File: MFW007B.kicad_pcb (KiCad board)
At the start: 4 copper layers, 84 x 42 mm, 63 parts, among them SW1 SW_Push, SW2 SW_Push, SW3 SW_Push, SW4 SW_Push, U1 24AA02-OT, U2 W5500, U3 STM32F103C8T6, Y1 25MHz

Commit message: update 2021-03-25
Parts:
- added U4: XC6206P332MR-G-SOT23, Package_TO_SOT_SMD:SOT-23, F.Cu at (169.0, 42.0)
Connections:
- net no_connect_(U3-Pad3) renamed /MCU/OSC32_IN
- net no_connect_(U3-Pad4) renamed /MCU/OSC32_OUT
- net no_connect_(U3-Pad5) renamed /MCU/OSC_IN
- net no_connect_(U3-Pad6) renamed /MCU/OSC_OUT

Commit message: fix label assignments and add 2x7 header
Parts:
- added J1: Conn_01x04, Connector_PinHeader_2.54mm:PinHeader_1x04_P2.54mm_Vertical, F.Cu at (170.5, 105.5)
- added J2: Conn_02x07, Connector_PinHeader_2.54mm:PinHeader_2x07_P2.54mm_Vertical, F.Cu at (164.5, 116.8)
- added J3: 4P JST-SH, Connector_JST:JST_SH_SM04B-SRSS-TB_1x04-1MP_P1.00mm_Horizontal, F.Cu at (169.0, 89.2)
- added TP1: TAMPER-RTC, TestPoint:TestPoint_Keystone_5010-5014_Multipurpose, F.Cu at (134.8, 118.2)
- added U5: TPS23753APWR, TPS23753APWR:SOP65P640X120-14N, F.Cu at (41.5, 42.5)
- moved U3 60.2 mm to (151.2, 107.5), turned to 180 degrees
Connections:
- net no_connect_(U3-Pad10) renamed /MCU/PA0_WKUP
- net no_connect_(U3-Pad20) renamed /MCU/BOOT1
- net no_connect_(U3-Pad44) renamed /MCU/BOOT0
- net no_connect_(U3-Pad7) renamed /MCU/NRST
- C10 pad 1: no_connect_(C10-Pad1) -> /CD
- JIO1 pad A6: no_connect_(JIO1-PadA6) -> /USBDP
- JIO1 pad A7: no_connect_(JIO1-PadA7) -> /USBDN
- JIO1 pad B6: no_connect_(JIO1-PadB6) -> /USBDP
- JIO1 pad B7: no_connect_(JIO1-PadB7) -> /USBDN
- JIO2 pad 3: no_connect_(JIO2-Pad3) -> /CD
- R11 pad 1: no_connect_(R11-Pad1) -> +3V3
- R11 pad 2: no_connect_(R11-Pad2) -> /CD
- R4 pad 2: /Ethernet MAC PHY/SDA -> /I2C1_SDA
- R5 pad 2: /Ethernet MAC PHY/SCL -> /I2C1_SCL
- U1 pad 1: /Ethernet MAC PHY/SCL -> /I2C1_SCL
- U1 pad 3: /Ethernet MAC PHY/SDA -> /I2C1_SDA
- U3 pad 14: no_connect_(U3-Pad14) -> /Ethernet MAC PHY/CS
- U3 pad 15: no_connect_(U3-Pad15) -> /Ethernet MAC PHY/SCLK
- U3 pad 16: no_connect_(U3-Pad16) -> /Ethernet MAC PHY/MISO
- U3 pad 17: no_connect_(U3-Pad17) -> /Ethernet MAC PHY/MOSI
- U3 pad 18: no_connect_(U3-Pad18) -> /Ethernet MAC PHY/IRQ
- U3 pad 2: no_connect_(U3-Pad2) -> Net-(U3-Pad2)
- U3 pad 21: no_connect_(U3-Pad21) -> /I2C2_SCL
- U3 pad 22: no_connect_(U3-Pad22) -> /I2C2_SDA
- U3 pad 25: no_connect_(U3-Pad25) -> /SPI2_CS
- U3 pad 26: no_connect_(U3-Pad26) -> /SPI2_SCK
- U3 pad 27: no_connect_(U3-Pad27) -> /SPI2_MISO
- U3 pad 28: no_connect_(U3-Pad28) -> /SPI2_MOSI
- U3 pad 29: no_connect_(U3-Pad29) -> /USER_SW_1
- U3 pad 30: no_connect_(U3-Pad30) -> /USER_SW_2
- U3 pad 31: no_connect_(U3-Pad31) -> /USER_SW_3
- U3 pad 32: no_connect_(U3-Pad32) -> /USBDN
- U3 pad 33: no_connect_(U3-Pad33) -> /USBDP
- U3 pad 34: no_connect_(U3-Pad34) -> /MCU/SWO
- U3 pad 37: no_connect_(U3-Pad37) -> /MCU/SWCLK
- U3 pad 42: no_connect_(U3-Pad42) -> /I2C1_SCL
- U3 pad 43: no_connect_(U3-Pad43) -> /I2C1_SDA

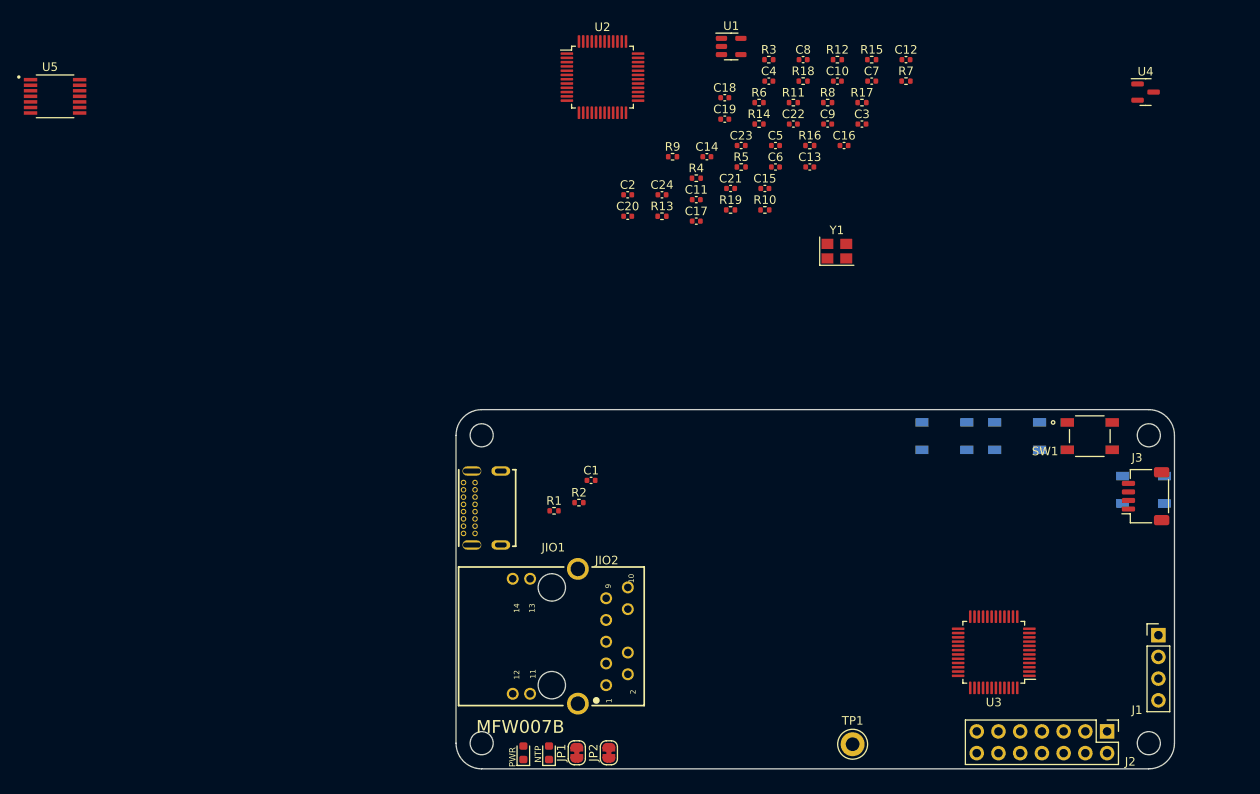
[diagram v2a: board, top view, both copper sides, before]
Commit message: rough component placement
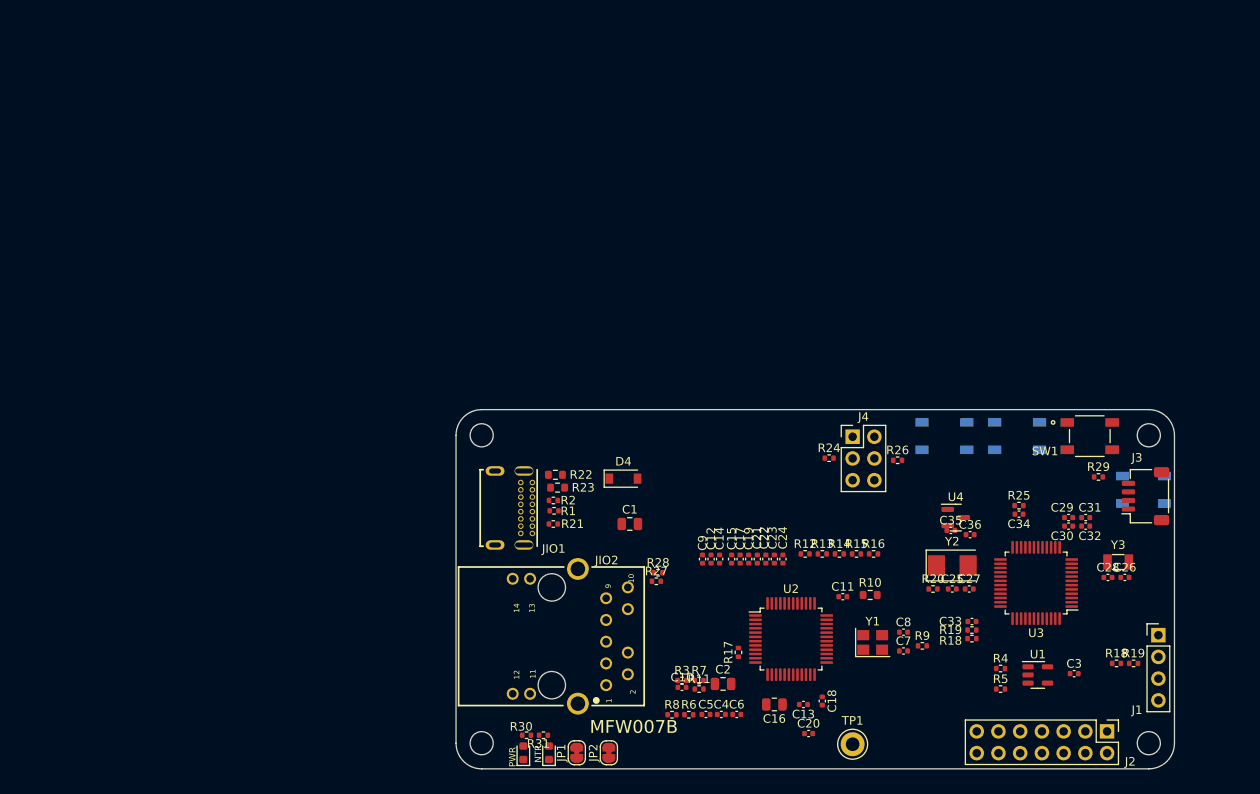
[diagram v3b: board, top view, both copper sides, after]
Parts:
- removed U5: TPS23753APWR, TPS23753APWR:SOP65P640X120-14N
- added C25: 20pF, Capacitor_SMD:C_0402_1005Metric, F.Cu at (146.4, 100.1)
- added C26: 20pF, Capacitor_SMD:C_0402_1005Metric, F.Cu at (166.6, 98.8)
- added C27: 20pF, Capacitor_SMD:C_0402_1005Metric, F.Cu at (148.4, 100.1)
- added C28: 20pF, Capacitor_SMD:C_0402_1005Metric, F.Cu at (164.6, 98.8)
- added C29: 100nF, Capacitor_SMD:C_0402_1005Metric, F.Cu at (160.0, 91.8)
- added C30: 100nF, Capacitor_SMD:C_0402_1005Metric, F.Cu at (160.0, 92.8)
- added C31: 100nF, Capacitor_SMD:C_0402_1005Metric, F.Cu at (162.0, 91.8)
- added C32: 100nF, Capacitor_SMD:C_0402_1005Metric, F.Cu at (162.0, 92.8)
- added C33: 100nF, Capacitor_SMD:C_0402_1005Metric, F.Cu at (148.7, 103.9)
- added C34: 1uF, Capacitor_SMD:C_0402_1005Metric, F.Cu at (154.2, 91.3)
- added C35: 1uF, Capacitor_SMD:C_0402_1005Metric, F.Cu at (146.2, 93.2)
- added C36: 1uF, Capacitor_SMD:C_0402_1005Metric, F.Cu at (148.5, 93.8)
- added D4: B5819W, Diode_SMD:D_SOD-123, F.Cu at (108.0, 87.2)
- added J4: Conn_02x03, Connector_PinHeader_2.54mm:PinHeader_2x03_P2.54mm_Vertical, F.Cu at (134.8, 82.3)
- added R18: 10K, Resistor_SMD:R_0402_1005Metric, F.Cu at (148.7, 105.9)
- added R19: 10K, Resistor_SMD:R_0402_1005Metric, F.Cu at (148.7, 104.9)
- added R20: 1M, Resistor_SMD:R_0402_1005Metric, F.Cu at (144.2, 100.1)
- added R21: 1.5K, Resistor_SMD:R_0402_1005Metric, F.Cu at (99.8, 92.5)
- added R22: 20R, Resistor_SMD:R_0603_1608Metric, F.Cu at (100.0, 86.8)
- added R23: 20R, Resistor_SMD:R_0603_1608Metric, F.Cu at (100.2, 88.2)
- added R24: 100K, Resistor_SMD:R_0402_1005Metric, F.Cu at (132.0, 84.8)
- added R25: 10K, Resistor_SMD:R_0402_1005Metric, F.Cu at (154.2, 90.3)
- added R26: 100K, Resistor_SMD:R_0402_1005Metric, F.Cu at (140.0, 85.0)
- added R27: 1K, Resistor_SMD:R_0402_1005Metric, F.Cu at (111.8, 99.2)
- added R28: 1K, Resistor_SMD:R_0402_1005Metric, F.Cu at (112.0, 98.2)
- added R29: 330, Resistor_SMD:R_0402_1005Metric, F.Cu at (163.5, 87.0)
- added R30: 330, Resistor_SMD:R_0402_1005Metric, F.Cu at (96.6, 117.2)
- added R31: 330, Resistor_SMD:R_0402_1005Metric, F.Cu at (98.6, 117.2)
- added Y2: 8MHz, Crystal:Crystal_SMD_5032-2Pin_5.0x3.2mm, F.Cu at (146.4, 97.3)
- added Y3: 32.768KHz, Crystal:Crystal_SMD_3215-2Pin_3.2x1.5mm, F.Cu at (165.8, 97.0)
- C1, C16, C2: footprint Capacitor_SMD:C_0402_1005Metric -> Capacitor_SMD:C_0805_2012Metric
- R10: footprint Resistor_SMD:R_0402_1005Metric -> Resistor_SMD:R_0603_1608Metric
- R18, R19: value 330R -> 10K
- moved U1 81.8 mm to (156.4, 110.2)
- moved R18 77.3 mm to (165.6, 108.8)
- moved C4 74.3 mm to (119.4, 114.8)
- moved R7 74.1 mm to (116.8, 110.8)
- moved R8 73.8 mm to (113.6, 114.8)
- moved R3 73.3 mm to (114.8, 110.8)
- moved C10 73.2 mm to (114.8, 111.6)
- moved R6 72.0 mm to (115.6, 114.8)
- moved C18 71.5 mm to (131.2, 113.2), turned to -90 degrees
- moved R19 70.9 mm to (167.6, 108.8)
- moved R11 69.4 mm to (116.8, 111.8)
- moved U2 69.3 mm to (127.5, 106.0)
- moved C3 68.9 mm to (160.7, 110.0)
- moved R5 68.2 mm to (152.1, 111.8)
- moved C8 68.0 mm to (140.7, 105.2)
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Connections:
- net /MCU/PA0_WKUP renamed no_connect_(U3-Pad10)
- D1 pad 4: /RGB_LED -> Net-(D1-Pad4)
- D2 pad 1: no_connect_(D2-Pad1) -> Net-(D2-Pad1)
- D2 pad 2: no_connect_(D2-Pad2) -> +3V3
- D3 pad 1: no_connect_(D3-Pad1) -> Net-(D3-Pad1)
- D3 pad 2: no_connect_(D3-Pad2) -> /NTP_LED
- JIO1 pad A4: +5V -> Net-(JIO1-PadA4)
- JIO1 pad A9: +5V -> Net-(JIO1-PadA4)
- JIO1 pad B4: +5V -> Net-(JIO1-PadA4)
- JIO1 pad B9: +5V -> Net-(JIO1-PadA4)
- JIO2 pad 11: /ETHLED1P -> Net-(JIO2-Pad11)
- JIO2 pad 12: /ETHLED1N -> Net-(JIO2-Pad12)
- JIO2 pad 13: /ETHLED2P -> Net-(JIO2-Pad11)
- JIO2 pad 14: /ETHLED2N -> Net-(JIO2-Pad14)
- JP1 pad 1: no_connect_(JP1-Pad1) -> +3V3
- JP1 pad 2: no_connect_(JP1-Pad2) -> Net-(JIO2-Pad11)
- JP2 pad 1: no_connect_(JP2-Pad1) -> /STLEDGND
- JP2 pad 2: no_connect_(JP2-Pad2) -> GND
- R18 pad 1: /ETHLINKLED -> /MCU/SWO
- R18 pad 2: /Ethernet MAC PHY/LINKLED -> GND
- R19 pad 1: /ETHACTLED -> +3V3
- R19 pad 2: /Ethernet MAC PHY/ACTLED -> /MCU/SWCLK
- U2 pad 25: /Ethernet MAC PHY/LINKLED -> /ETHLINKLED
- U2 pad 27: /Ethernet MAC PHY/ACTLED -> /ETHACTLED
- U3 pad 19: no_connect_(U3-Pad19) -> /RGB_LED
- U3 pad 23: Net-(U3-Pad23) -> GND
- U3 pad 24: Net-(U3-Pad24) -> +3V3
- U3 pad 35: Net-(U3-Pad23) -> GND
- U3 pad 36: Net-(U3-Pad24) -> +3V3
- U3 pad 41: no_connect_(U3-Pad41) -> /NTP_LED
- U3 pad 47: Net-(U3-Pad23) -> GND
- U3 pad 48: Net-(U3-Pad24) -> +3V3
- U3 pad 7: /MCU/NRST -> /RESET_SW
- U3 pad 8: no_connect_(U3-Pad8) -> GND
- U3 pad 9: no_connect_(U3-Pad9) -> +3V3

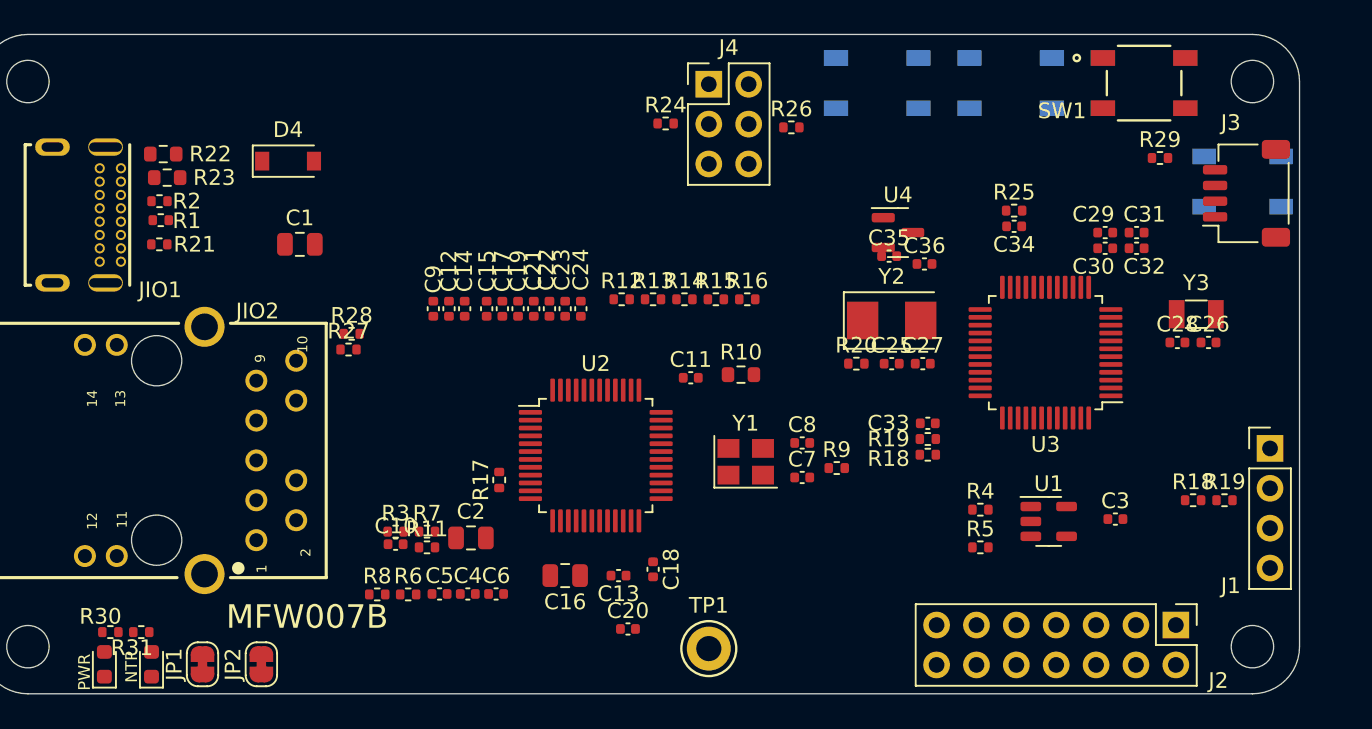
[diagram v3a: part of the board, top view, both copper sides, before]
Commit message: refining component placement
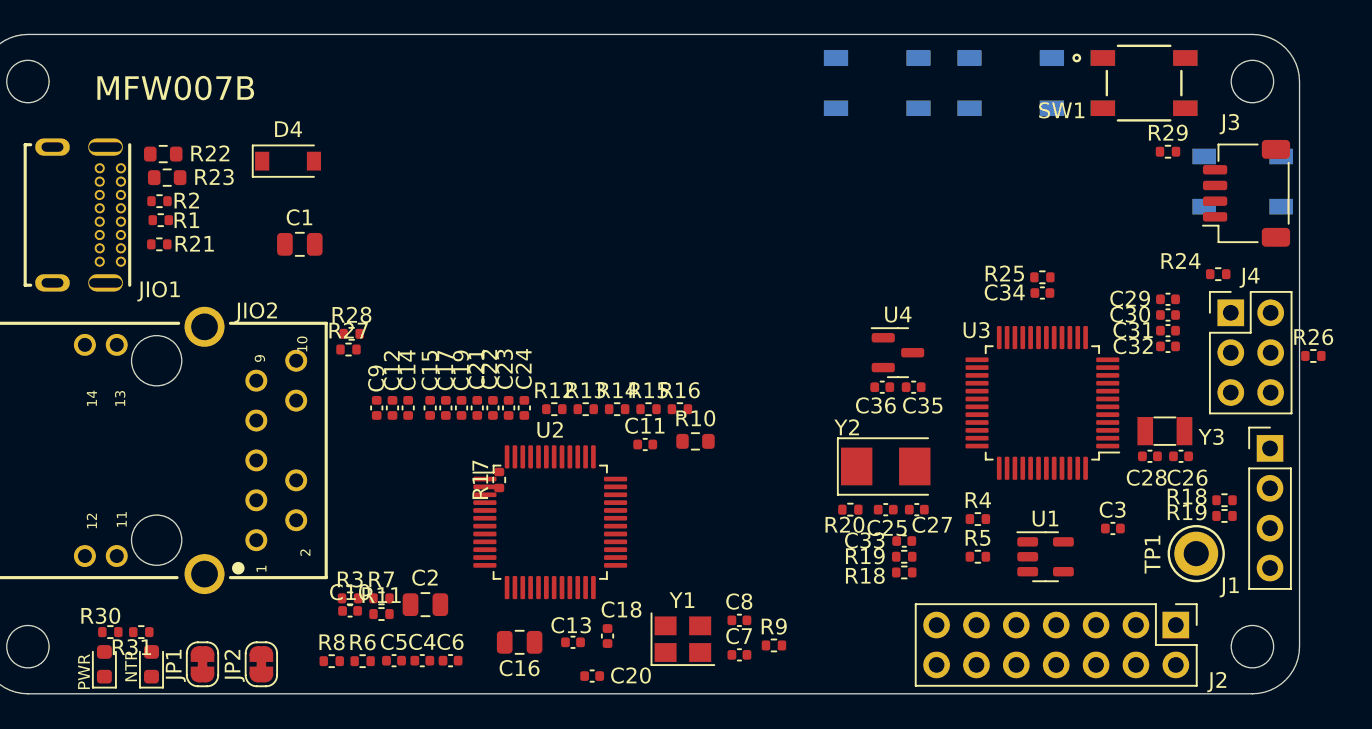
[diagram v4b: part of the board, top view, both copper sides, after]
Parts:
- moved R24 36.5 mm to (167.2, 94.4)
- moved J4 36.3 mm to (168.0, 96.9)
- moved R26 36.3 mm to (173.3, 99.6)
- moved TP1 31.6 mm to (165.8, 112.2), turned to 90 degrees
- moved C7 12.0 mm to (136.7, 118.7)
- moved Y1 12.0 mm to (133.1, 117.7)
- moved C8 12.0 mm to (136.7, 116.5)
- moved R9 12.0 mm to (138.9, 118.0)
- moved C25 9.31 mm to (146.0, 109.4)
- moved C27 9.31 mm to (148.0, 109.4)
- moved R20 9.31 mm to (143.8, 109.4)
- moved Y2 9.31 mm to (146.0, 106.7)
- moved C35 8.49 mm to (147.8, 101.6), turned to 180 degrees
- moved C36 8.30 mm to (145.8, 101.6)
- moved R12 8.21 mm to (124.9, 103.0)
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
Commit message: start routing
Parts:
- moved J2 40.6 mm to (132.0, 92.5)
- moved C29 21.9 mm to (142.8, 101.6), turned to 90 degrees
- moved C30 20.7 mm to (143.8, 101.6), turned to 90 degrees
- moved C31 19.5 mm to (144.8, 101.6), turned to 90 degrees
- moved C32 18.4 mm to (145.8, 101.6), turned to 90 degrees
- moved C27 15.8 mm to (163.4, 105.8)
- moved Y2 15.8 mm to (161.4, 103.0)
- moved C25 15.7 mm to (161.3, 105.8)
- moved R20 11.8 mm to (155.5, 108.2), turned to 90 degrees
- moved U4 10.4 mm to (146.9, 89.0)
- moved C35 10.4 mm to (147.9, 91.2)
- moved C36 10.4 mm to (145.9, 91.2)
- moved R4 9.97 mm to (147.4, 118.9)
- moved TP1 9.30 mm to (158.5, 118.0)
- moved R16 8.71 mm to (124.2, 102.9), turned to 90 degrees
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- renumbered SW1 to RESET
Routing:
- net /NTP_LED: track 0.00 -> 61.3 mm, vias 0 -> 2
- net /USBDP: track 0.00 -> 51.5 mm
- net /USBDN: track 0.00 -> 48.8 mm
- net /RESET_SW: track 0.00 -> 32.8 mm
- net /Ethernet MAC PHY/MOSI: track 0.00 -> 28.3 mm, vias 0 -> 2
- net /Ethernet MAC PHY/IRQ: track 0.00 -> 26.8 mm, vias 0 -> 2
- net /RGB_LED: track 0.00 -> 23.3 mm, vias 0 -> 2
- net /Ethernet MAC PHY/SCLK: track 0.00 -> 19.9 mm, vias 0 -> 1
- net /V1P: track 0.00 -> 19.3 mm
- net /Ethernet MAC PHY/MISO: track 0.00 -> 18.5 mm, vias 0 -> 1
- net /V2P: track 0.00 -> 14.5 mm
- net /V1N: track 0.00 -> 13.9 mm
- net /Ethernet MAC PHY/CS: track 0.00 -> 13.0 mm
- net /STLEDGND: track 0.00 -> 12.2 mm, vias 0 -> 2
- net Net-(JIO1-PadA4): track 0.00 -> 11.2 mm
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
